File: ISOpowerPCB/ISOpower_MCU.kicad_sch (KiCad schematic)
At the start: 5 parts

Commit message: deleted old backups & added documentation
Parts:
- removed J?: USB_B_Mini, symbol Connector:USB_B_Mini
- removed U? (x2): CH340C, Package_SO:SOIC-16_3.9x9.9mm_P1.27mm, symbol Interface_USB:CH340C
- added C? (x3): 100N, Capacitor_SMD:C_0805_2012Metric_Pad1.18x1.45mm_HandSolder, symbol 000_Capacitor_film_immo:cap_film_0805
- added C? (x2): 22p, Capacitor_SMD:C_0805_2012Metric_Pad1.18x1.45mm_HandSolder, symbol 000_Capacitor_film_immo:cap_film_0805
- added D?: LED_0805_smd, Diode_SMD:D_0805_2012Metric_Pad1.15x1.40mm_HandSolder, symbol 000_Diodes_Immo:LED_0805_smd
- added J?: PCB_PIN_header_male, symbol Connector:Conn_01x03_Male
- added J?: AVR-ISP-6, symbol Connector:AVR-ISP-6
- added JP?: Jumper_3_Bridged12, symbol 000_Connectors_Immo:Jumper_3_Bridged12
- added L?: L, symbol Device:L
- added R? (x2): 10k, Resistor_SMD:R_0805_2012Metric_Pad1.20x1.40mm_HandSolder, symbol 000_Resistors_Immo:Resistor_0805
- added SW?: SW_Push, symbol Switch:SW_Push
- added TP?: TestPoint, symbol Connector:TestPoint
- added Y?: 16MHz, symbol Device:Crystal_GND24
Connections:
- net +3.3VA: now also C?.2
- net +5VD: now also C?.1, J?.3 (Pin_3), JP?.1 (A); no longer U?.4 (VCC), U?.6 (VCC)
- net CH_A: now also U?.32 (PD2); no longer U?.30 (PD0)
- net CH_B: now also U?.1 (PD3); no longer U?.31 (PD1)
- net CH_C: now also U?.2 (PD4); no longer U?.32 (PD2)
- net CH_D: now also U?.9 (PD5); no longer U?.1 (PD3)
- net CH_E: now also U?.10 (PD6); no longer U?.2 (PD4)
- net GND1: now also C?.1, C?.2, C?.2, C?.2, J?.6 (GND), L?.2, R?.2, SW?.2
- net Logic Level Conversion/1B: now reaches U?.34 (RXD0/IO3)
- net Logic Level Conversion/0B: now reaches U?.35 (TXD0/IO1)
- net at U?.11 (PD7): now also D?.2 (A)
- net SSERIAL_TX: now reaches U?.12 (PB0)
- net SSERIAL_RX: now reaches U?.13 (PB1)
- net at U?.15 (PB3): now also J?.4 (MOSI)
- net at U?.16 (PB4): now also J?.1 (MISO)
- net at U?.17 (PB5): now also J?.3 (SCK)
- net at U?.18 (AVCC): now also C?.2, L?.1
- net ADC0: now reaches U?.23 (PC0)
- net ADC1: now reaches U?.24 (PC1)
- net ADC2: now reaches U?.25 (PC2)
- net ADC3: now reaches U?.26 (PC3)
- net ADC4: now reaches U?.27 (PC4)
- net ADC5: now reaches U?.28 (PC5)
- net USB MCU Interface/DTR_A: now reaches U?.29 (~{RESET}/PC6)
- net USB MCU Interface/DTR_A: now also J?.5 (~{RST}), R?.2, SW?.1, TP?.1
- net at U?.7 (XTAL1/PB6): now also C?.1, Y?.1
- net at U?.8 (XTAL2/PB7): now also C?.1, Y?.3
- new net: D?.1 (K), R?.1
- new net MCU_5V_BUS: C?.1, J?.2 (Pin_2), JP?.2 (C), R?.1, U?.4 (VCC), U?.6 (VCC)
- new net USB MCU Interface/RxD_A: U?.30 (PD0)
- new net USB MCU Interface/TxD_A: U?.31 (PD1)
- new net USB_power_bus: J?.1 (Pin_1), J?.2 (VCC), JP?.3 (B)
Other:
- added sheet Logic Level Conversion (logiclevelconverter.kicad_sch)
- added sheet USB MCU Interface (A_usb_interface.kicad_sch)
- added sheet USB MCU Interface B (B_usb_interface.kicad_sch)
- note added: "3.3v USB Interface"
- note added: "5v USB Interface"
- note added: "For normal use, jumped is left in the 5v Bus Configuration, For Advanced users: Jumper can be moved to USB_power_bus during programming to avoid the need to power the entire system."
- note added: "MCU decoupling caps"
- note added: "MCU power Distribution"
- note added: "Programming Power Routing"
- note added: "USB power routed to its own bus, to allow potential for USB power to be used for powering microcontrollers during programming, but avoid case where user inadvertently tries to power entire 5v BUS from USB rail"
- moved on the sheet: U?

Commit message: modified pcb files
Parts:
- removed U?: ESP32-WROOM-32, RF_Module:ESP32-WROOM-32, symbol RF_Module:ESP32-WROOM-32
- added J?: PCB_PIN_header_male, symbol Connector:Conn_01x03_Male
- added U?: ESP32-WROOM-32, RF_Module:ESP32-WROOM-32, symbol 000_MCU_microcontrollers_Immo:ESP32-WROOM-32
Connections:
- net +3.3VA: now also U?.2 (VDD)
- net GND1: now also U?.1 (GND)
- net Logic Level Conversion/0B: now also U?.28 (UART2_TX/GPIO17)
- net Logic Level Conversion/1B: now also U?.27 (UART2_RX/GPIO16)
- net USB MCU Interface B/RxD_B: now also U?.35 (TXD0/GPIO1)
- net USB MCU Interface B/TxD_B: now also U?.34 (RXD0/GPIO3)
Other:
- sheet USB MCU Interface renamed USB MCU Interface A
- sheet USB MCU Interface A ports: added none; removed DTR_B, RxD_B, TxD_B
- sheet USB MCU Interface B ports: added none; removed DTR_A, RxD_A, TxD_A
- moved on the sheet: C?, D?, J?, JP?, L?, R?, SW?, TP?, U?, Y?

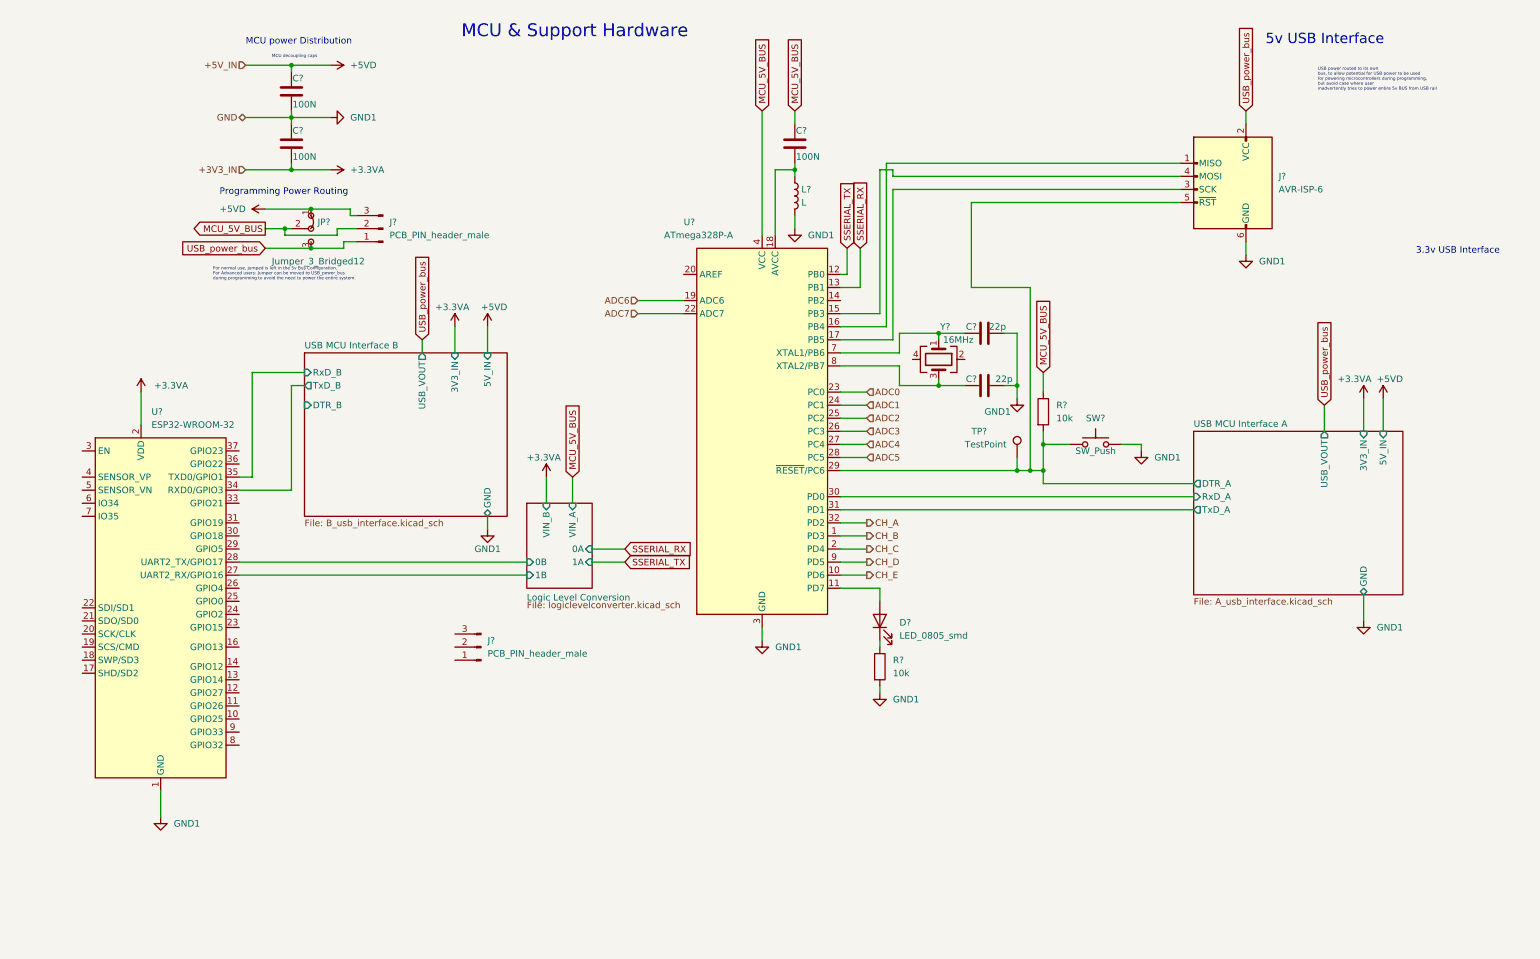
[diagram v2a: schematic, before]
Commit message: Finished initial circuit design
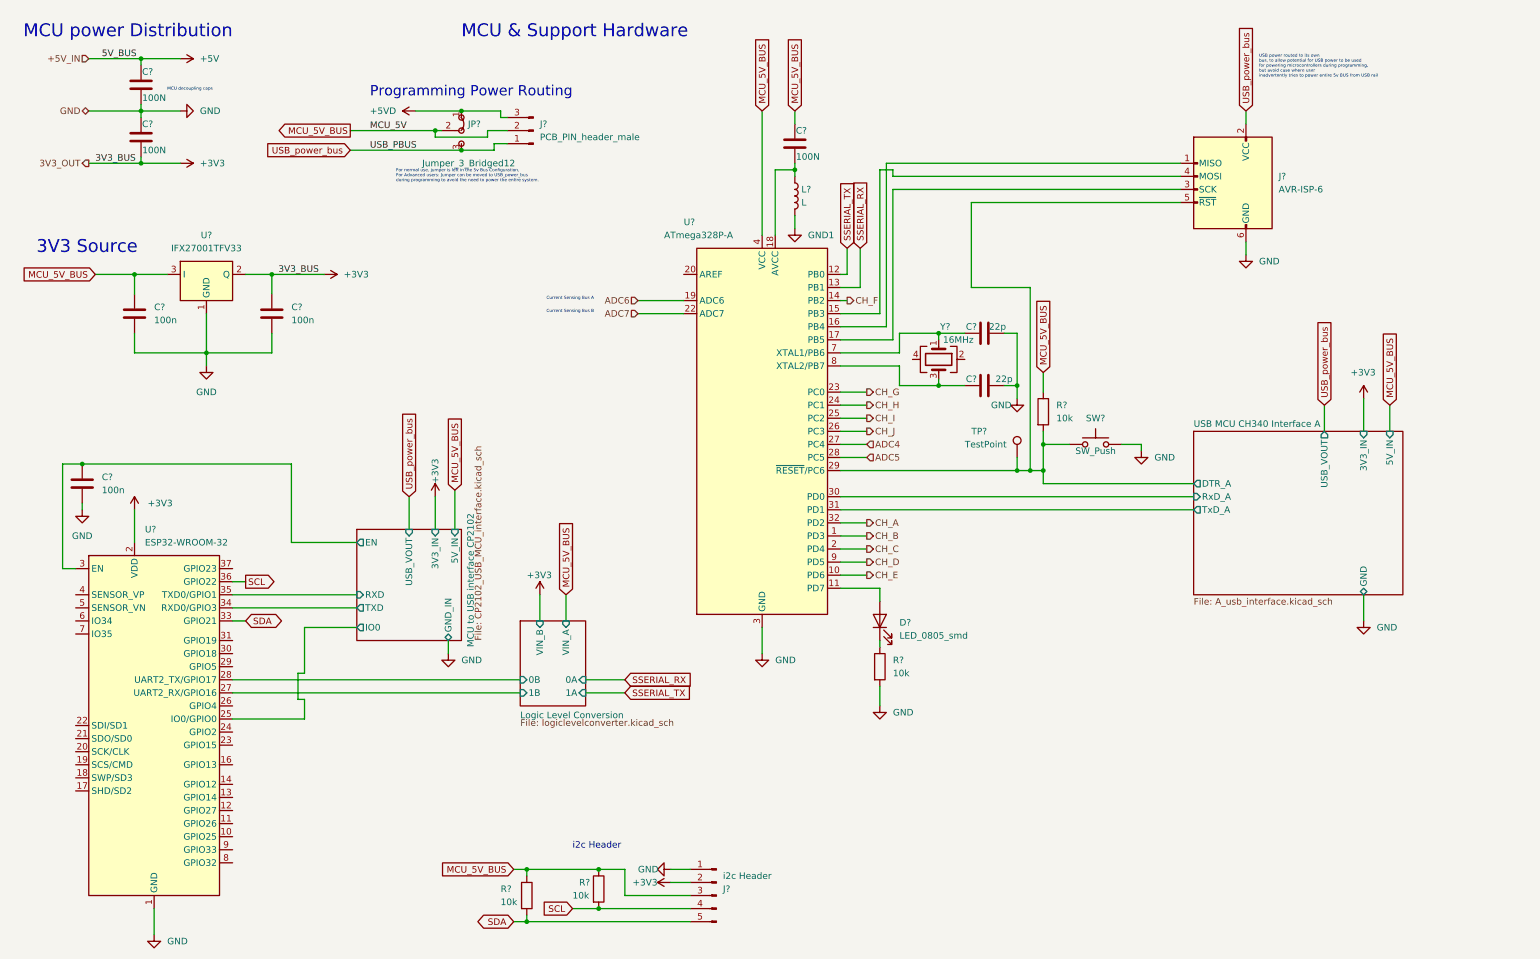
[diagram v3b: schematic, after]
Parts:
- removed J?: PCB_PIN_header_male, symbol Connector:Conn_01x03_Male
- added C? (x3): 100n, Capacitor_SMD:C_0805_2012Metric_Pad1.18x1.45mm_HandSolder, symbol 000_Capacitor_film_immo:cap_film_0805
- added J?: i2c Header, symbol Connector:Conn_01x05_Male
- added R? (x2): 10k, Resistor_SMD:R_0805_2012Metric_Pad1.20x1.40mm_HandSolder, symbol 000_Resistors_Immo:Resistor_0805
- added U?: IFX27001TFV33, Package_TO_SOT_SMD:TO-252-3_TabPin2, symbol Regulator_Linear:IFX27001TFV33
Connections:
- net +5VD: no longer C?.1
- net GND1: no longer C?.1, C?.2, C?.2, C?.2, J?.6 (GND), R?.2, SW?.2, U?.1 (GND), U?.21 (GND), U?.3 (GND), U?.5 (GND)
- net MCU_5V_BUS: now also C?.1, J?.3 (Pin_3), R?.1, R?.1, U?.3 (I)
- net CH_F: now reaches U?.14 (PB2)
- net MCU to USB interface CP2102/IO0: now reaches U?.25 (IO0/GPIO0)
- net MCU to USB interface CP2102/EN: now reaches U?.3 (EN)
- net MCU to USB interface CP2102/EN: now also C?.1
- net SDA: now reaches U?.33 (GPIO21)
- net SDA: now also J?.5 (Pin_5), R?.2
- net SCL: now reaches U?.36 (GPIO22)
- net SCL: now also J?.4 (Pin_4), R?.2
- net +3.3VA renamed +3V3
- net +3V3: now also C?.1, J?.2 (Pin_2), U?.2 (Q)
- net ADC0 renamed CH_G
- net ADC1 renamed CH_H
- net ADC2 renamed CH_I
- net ADC3 renamed CH_J
- net USB MCU Interface B/RxD_B renamed MCU to USB interface CP2102/RXD
- net USB MCU Interface B/TxD_B renamed MCU to USB interface CP2102/TXD
- new net +5V: C?.1
- new net GND: C?.1, C?.2, C?.2, C?.2, C?.2, C?.2, C?.2, J?.1 (Pin_1), J?.6 (GND), R?.2, SW?.2, U?.1 (GND), U?.1 (GND), U?.21 (GND), U?.3 (GND), U?.5 (GND)
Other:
- sheet USB MCU Interface A renamed USB MCU CH340 Interface A
- removed sheet USB MCU Interface B
- added sheet MCU to USB interface CP2102 (CP2102_USB_MCU_interface.kicad_sch)
- note added: "3V3 Source"
- note added: "Current Sensing Bus A"
- note added: "Current Sensing Bus B"
- note added: "For normal use, jumper is left in the 5v Bus Configuration, For Advanced users: Jumper can be moved to USB_power_bus during programming to avoid the need to power the entire system."
- note added: "i2c Header"
- note removed: "3.3v USB Interface"
- note removed: "5v USB Interface"
- note removed: "For normal use, jumped is left in the 5v Bus Configuration, For Advanced users: Jumper can be moved to USB_power_bus during programming to avoid the need to power the entire system."
- moved on the sheet: C?, J?, JP?, U?

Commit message: PCB Notes added
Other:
- note added: "ADD BOOT AND EN SWITCHES"
- note added: "CHANGE TO CH430"
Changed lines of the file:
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@@
     (effects (font (size 0.6 0.6)) (justify left bottom))
+  )
+  (text "CHANGE TO CH430" (at 72.39 138.43 0)
+    (effects (font (size 2.5 2.5)) (justify left bottom))
   )
   (text "Current Sensing Bus B" (at 115.57 71.12 0)
@@
     (effects (font (size 2.5 2.5)) (justify left bottom))
   )
+  (text "ADD BOOT AND EN SWITCHES" (at 66.04 113.03 0)
+    (effects (font (size 2.5 2.5)) (justify left bottom))
+  )

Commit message: Major schematic revisions
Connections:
- net +5V is gone; now on net MCU_5V_BUS: C?.1
- net +5VD is gone; now on net MCU_5V_BUS: J?.3 (Pin_3), JP?.1 (A)
- net MCU_5V_BUS: now also J?.2 (VCC)
- net MCU to USB interface CP2102/EN renamed USB ESP32 CH340 Interface /ESP_EN
- net MCU to USB interface CP2102/IO0 renamed USB ESP32 CH340 Interface /ESP_IO0
- net MCU to USB interface CP2102/RXD renamed USB ESP32 CH340 Interface /RxD_B
- net MCU to USB interface CP2102/TXD renamed USB ESP32 CH340 Interface /TxD_B
- net USB_power_bus renamed USB_PBUS
- net USB_PBUS: no longer J?.2 (VCC)
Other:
- removed sheet MCU to USB interface CP2102
- added sheet USB ESP32 CH340 Interface  (ch340_ESP32.kicad_sch)
- note removed: "CHANGE TO CH430"
- moved on the sheet: C?, J?, JP?

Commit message: significant changes
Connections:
- net CH_D renamed IN_D
- net CH_E renamed IN_E
- net Logic Level Conversion/0B renamed Logic Level Conversion/0A
- net Logic Level Conversion/1B renamed Logic Level Conversion/1A
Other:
- sheet Logic Level Conversion ports: added 3V3_IN, 5V_IN, GND, OE; removed VIN_A, VIN_B
- note added: "For normal use, jumper is left in the 5v Bus Configuration, For Advanced users: Jumper can be moved to USB_power_bus, to avoid the need to power the entire system, during programming."
- note removed: "ADD BOOT AND EN SWITCHES"
- note removed: "For normal use, jumper is left in the 5v Bus Configuration, For Advanced users: Jumper can be moved to USB_power_bus during programming to avoid the need to power the entire system."
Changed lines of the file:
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@@
   (junction (at 191.77 85.09) (diameter 0) (color 0 0 0 0)
   )
+  (junction (at 54.61 142.24) (diameter 0) (color 0 0 0 0)
+  )
   (junction (at 36.83 35.56) (diameter 0) (color 0 0 0 0)
   )
@@
     (stroke (width 0) (type default) (color 0 0 0 0))
   )
+  (wire (pts (xy 54.61 142.24) (xy 115.57 142.24))
+    (stroke (width 0) (type default) (color 0 0 0 0))
+  )
   (wire (pts (xy 54.61 130.81) (xy 57.15 130.81))
     (stroke (width 0) (type default) (color 0 0 0 0))
@@
     (stroke (width 0) (type default) (color 0 0 0 0))
   )
+  (wire (pts (xy 54.61 144.78) (xy 115.57 144.78))
+    (stroke (width 0) (type default) (color 0 0 0 0))
+  )
   (wire (pts (xy 36.83 35.56) (xy 44.45 35.56))
     (stroke (width 0) (type default) (color 0 0 0 0))
@@
     (stroke (width 0) (type default) (color 0 0 0 0))
   )
-  (wire (pts (xy 54.61 144.78) (xy 115.57 144.78))
-    (stroke (width 0) (type default) (color 0 0 0 0))
-  )
   (wire (pts (xy 54.61 149.86) (xy 68.58 149.86))
     (stroke (width 0) (type default) (color 0 0 0 0))
@@
     (stroke (width 0) (type default) (color 0 0 0 0))
   )
+  (wire (pts (xy 50.8 142.24) (xy 54.61 142.24))
+    (stroke (width 0) (type default) (color 0 0 0 0))
+  )
   (wire (pts (xy 62.23 63.5) (xy 62.23 67.31))
     (stroke (width 0) (type default) (color 0 0 0 0))
@@
   )
   (wire (pts (xy 157.48 31.75) (xy 157.48 55.88))
-    (stroke (width 0) (type default) (color 0 0 0 0))
-  )
-  (wire (pts (xy 54.61 142.24) (xy 115.57 142.24))
     (stroke (width 0) (type default) (color 0 0 0 0))
   )
@@
     (effects (font (size 0.6 0.6)) (justify left bottom))
   )
-  (text "For normal use, jumper is left in the 5v Bus Configuration,\nFor Advanced users: Jumper can be moved to USB_power_bus \nduring programming to avoid the need to power the entire system.\n"
-    (at 86.36 39.37 0)
+  (text "For normal use, jumper is left in the 5v Bus Configuration,\nFor Advanced users: Jumper can be moved to USB_power_bus, \nto avoid the need to power the entire system, \nduring programming.\n"
+    (at 86.36 40.64 0)
     (effects (font (size 0.6 0.6)) (justify left bottom))
   )
   (text "3V3 Source" (at 16.51 59.69 0)
-    (effects (font (size 2.5 2.5)) (justify left bottom))
-  )
-  (text "ADD BOOT AND EN SWITCHES" (at 20.32 97.79 0)
     (effects (font (size 2.5 2.5)) (justify left bottom))
   )
@@
     (effects (font (size 1.27 1.27)) (justify left))
   )
-  (hierarchical_label "CH_D" (shape output) (at 177.8 119.38 0)
+  (hierarchical_label "IN_D" (shape input) (at 177.8 119.38 0)
     (effects (font (size 1.27 1.27)) (justify left))
   )
@@
     (effects (font (size 1.27 1.27)) (justify left))
   )
-  (hierarchical_label "CH_E" (shape output) (at 177.8 121.92 0)
+  (hierarchical_label "IN_E" (shape input) (at 177.8 121.92 0)
     (effects (font (size 1.27 1.27)) (justify left))
   )
@@
       (effects (font (size 1.27 1.27)) (justify left top))
     )
-    (pin "1B" input (at 115.57 144.78 180)
-      (effects (font (size 1.27 1.27)) (justify left))
-    )
-    (pin "1A" input (at 128.27 144.78 0)
+    (pin "5V_IN" input (at 124.46 130.81 90)
       (effects (font (size 1.27 1.27)) (justify right))
     )
-    (pin "0B" input (at 115.57 142.24 180)
-      (effects (font (size 1.27 1.27)) (justify left))
-    )
-    (pin "0A" input (at 128.27 142.24 0)
+    (pin "3V3_IN" input (at 119.38 130.81 90)
       (effects (font (size 1.27 1.27)) (justify right))
     )
-    (pin "VIN_A" input (at 124.46 130.81 90)
+    (pin "GND" bidirectional (at 121.92 147.32 270)
+      (effects (font (size 1.27 1.27)) (justify left))
+    )
+    (pin "OE" input (at 128.27 139.7 0)
       (effects (font (size 1.27 1.27)) (justify right))
     )
-    (pin "VIN_B" input (at 119.38 130.81 90)
+    (pin "1B" bidirectional (at 128.27 144.78 0)
       (effects (font (size 1.27 1.27)) (justify right))
     )
-  )
+    (pin "1A" bidirectional (at 115.57 144.78 180)
+      (effects (font (size 1.27 1.27)) (justify left))
+    )
+    (pin "0B" bidirectional (at 128.27 142.24 0)
+      (effects (font (size 1.27 1.27)) (justify right))
+    )
+    (pin "0A" bidirectional (at 115.57 142.24 180)
+      (effects (font (size 1.27 1.27)) (justify left))
+    )
+  )
